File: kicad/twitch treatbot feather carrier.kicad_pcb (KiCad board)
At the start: 2 copper layers, 0 parts

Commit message: PCB floorplanning
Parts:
- added A1: Adafruit_Feather_HUZZAH_ESP8266, Module:Adafruit_Feather, F.Cu at (124.3, 100.4)
- added C1: 1000u/25V, Capacitor_THT:CP_Radial_D13.0mm_P5.00mm, F.Cu at (160.7, 133.2)
- added C2: 10u/25V, Capacitor_THT:CP_Radial_D8.0mm_P3.80mm, F.Cu at (198.0, 130.7)
- added C3: 10u, Capacitor_SMD:C_0805_2012Metric, F.Cu at (206.9, 131.9)
- added C4: 10u, Capacitor_SMD:C_0805_2012Metric, F.Cu at (197.2, 140.0)
- added C5: 1u, Capacitor_SMD:C_0805_2012Metric, F.Cu at (182.0, 158.8)
- added C6: 1000u/25V, Capacitor_THT:CP_Radial_D13.0mm_P5.00mm, F.Cu at (160.7, 147.8)
- added C7: 10u, Capacitor_SMD:C_0805_2012Metric, F.Cu at (197.2, 137.0)
- added C8: 10u, Capacitor_SMD:C_0805_2012Metric, F.Cu at (211.8, 127.4)
- added C9: 10u, Capacitor_SMD:C_0805_2012Metric, F.Cu at (197.2, 143.0)
- added D1: +12V, LED_SMD:LED_1206_3216Metric, F.Cu at (167.7, 156.7)
- added D2: +5V, LED_SMD:LED_1206_3216Metric, F.Cu at (182.6, 155.6)
- added D3: +3V3, LED_SMD:LED_1206_3216Metric, F.Cu at (167.7, 160.1)
- added J1: 128x64 OLED, Connector_PinSocket_2.54mm:PinSocket_1x04_P2.54mm_Vertical, F.Cu at (131.2, 149.9)
- added J2: Quiic MP3 Trigger [CHECK FOOTPRINT], Connector_PinSocket_2.54mm:PinSocket_1x04_P2.54mm_Vertical, F.Cu at (126.5, 149.4)
- added J3: M2, TerminalBlock:TerminalBlock_Altech_AK300-2_P5.00mm, F.Cu at (186.1, 132.9)
- added J4: M1, TerminalBlock:TerminalBlock_Altech_AK300-2_P5.00mm, F.Cu at (173.8, 146.9)
- added J5: NEO_PWR, TerminalBlock:TerminalBlock_Altech_AK300-2_P5.00mm, F.Cu at (186.1, 146.9)
- added J6: NEO_Signal, TerminalBlock:TerminalBlock_Altech_AK300-2_P5.00mm, F.Cu at (173.8, 132.9)
- added Q1: BSS138, Package_TO_SOT_SMD:SOT-23, F.Cu at (207.2, 128.2)
- added R1: 10k, Resistor_SMD:R_0805_2012Metric, F.Cu at (201.6, 142.8)
- added R2: 4k7, Resistor_SMD:R_0805_2012Metric, F.Cu at (211.8, 130.4)
- added R3: 1k, Resistor_SMD:R_0805_2012Metric, F.Cu at (186.4, 158.8)
- added R4: 10k, Resistor_SMD:R_0805_2012Metric, F.Cu at (187.6, 155.4)
- added R5: 1k, Resistor_SMD:R_0805_2012Metric, F.Cu at (216.3, 127.4)
- added R6: 1k, Resistor_SMD:R_0805_2012Metric, F.Cu at (206.9, 134.9)
- added R7: 10k, Resistor_SMD:R_0805_2012Metric, F.Cu at (201.6, 139.8)
- added RDNP1: 4k7, Resistor_SMD:R_0805_2012Metric, F.Cu at (197.2, 146.0)
- added SW1: ESP RESET, My Libraries:SW_Push_CK_PTS525_SM15, F.Cu at (175.1, 157.1)
- added SW2: Wiggle, My Libraries:SW_Push_CK_PTS525_SM15, F.Cu at (160.2, 158.2)
- added TP1: TestPoint_Harwin, My Libraries:Harwin-S1751-46-Test-Point, F.Cu at (201.6, 136.9)
- added U1: TMC2208_BREAKOUT, My Libraries:DIP-16_W12.7mm, F.Cu at (148.3, 95.3)

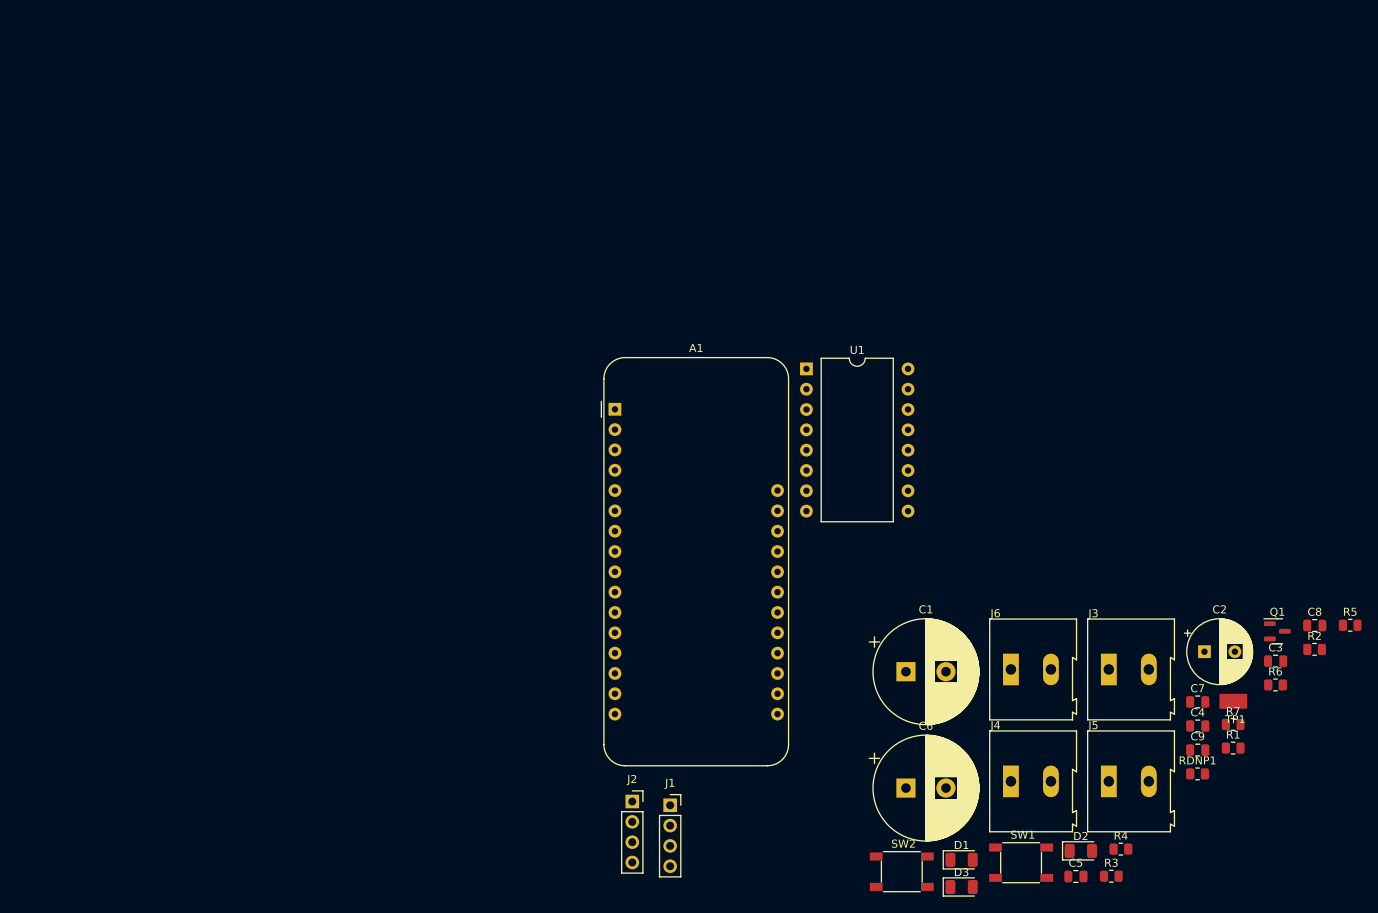
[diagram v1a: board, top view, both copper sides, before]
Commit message: first floorplan done
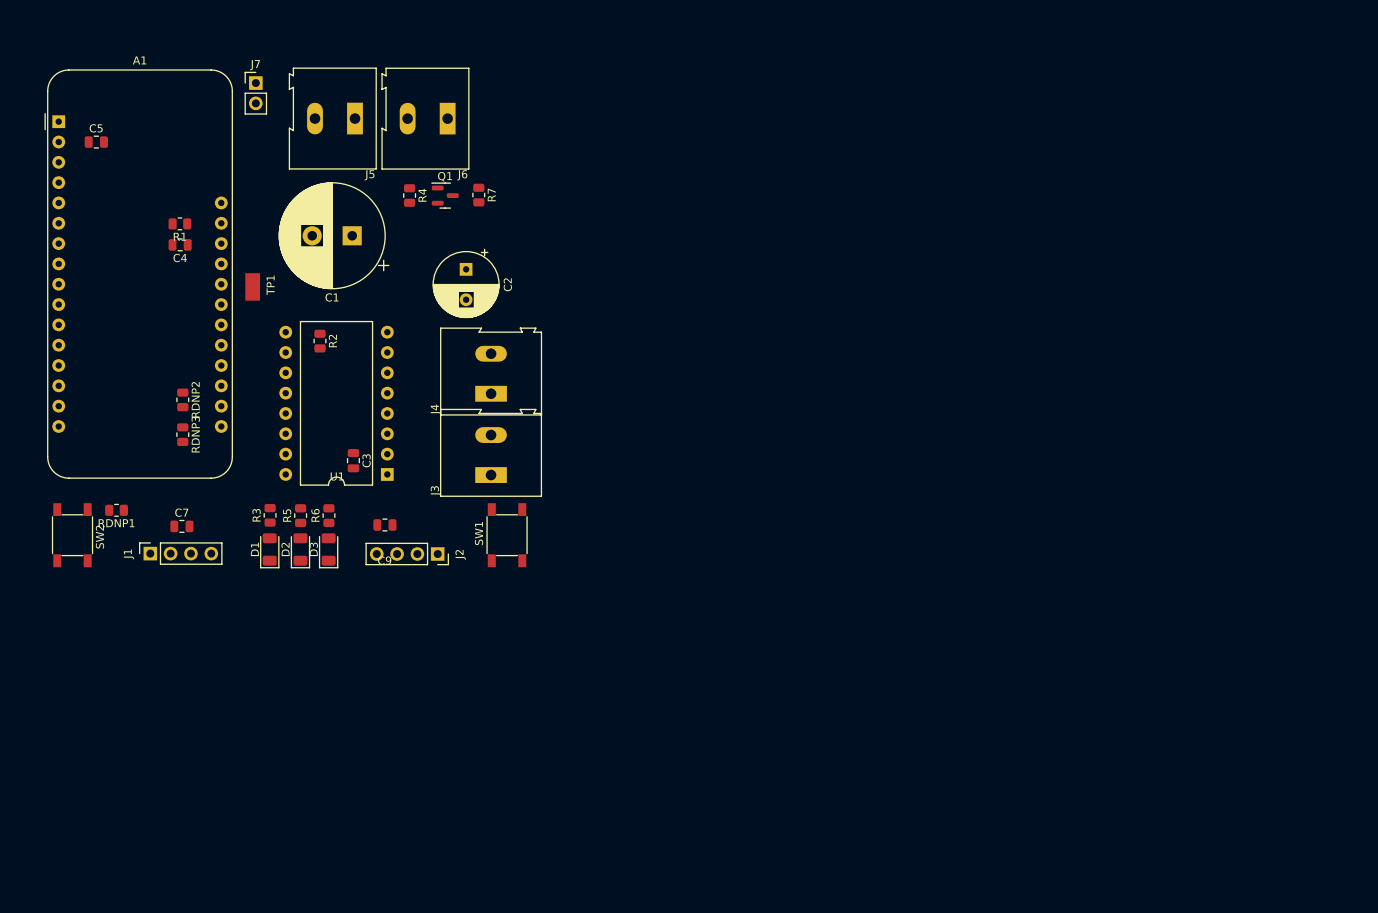
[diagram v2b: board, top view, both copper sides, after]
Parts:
- removed C6: 1000u/25V, Capacitor_THT:CP_Radial_D13.0mm_P5.00mm
- removed C8: 10u, Capacitor_SMD:C_0805_2012Metric
- added J7: +5V_IN, Connector_PinHeader_2.54mm:PinHeader_1x02_P2.54mm_Vertical, F.Cu at (79.5, 59.6)
- added RDNP2: 4k7, Resistor_SMD:R_0805_2012Metric, F.Cu at (70.3, 99.2)
- added RDNP3: 4k7, Resistor_SMD:R_0805_2012Metric, F.Cu at (70.3, 103.6)
- J5: value NEO_PWR -> +12V_IN
- moved C5 153.0 mm to (59.5, 67.0)
- moved R1 147.1 mm to (70.0, 77.2), turned to 180 degrees
- moved C4 140.7 mm to (70.0, 79.8), turned to 180 degrees
- moved RDNP1 139.1 mm to (62.0, 113.0), turned to 180 degrees
- moved TP1 133.1 mm to (79.1, 85.1), turned to 90 degrees
- moved R5 131.9 mm to (85.1, 113.7), turned to 90 degrees
- moved R2 130.2 mm to (87.5, 91.9), turned to -90 degrees
- moved C7 128.9 mm to (70.2, 115.0)
- moved J5 125.5 mm to (91.9, 64.1), turned to 180 degrees
- moved R4 120.8 mm to (98.7, 73.7), turned to -90 degrees
- moved R6 120.2 mm to (88.6, 113.7), turned to 90 degrees
- moved C3 118.0 mm to (91.7, 106.8), turned to -90 degrees
- moved Q1 117.4 mm to (103.1, 73.7)
- moved R7 115.2 mm to (107.3, 73.6), turned to -90 degrees
- moved R3 114.4 mm to (81.2, 113.7), turned to 90 degrees
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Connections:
- C9 pad 1: +5V -> +3V3
- J5 pad 1: +5V -> +12V

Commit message: 2nd floorplan
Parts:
- removed TP1: TestPoint_Harwin, My Libraries:Harwin-S1751-46-Test-Point
- moved A1 44.2 mm to (74.5, 104.0), turned to 180 degrees
- moved RDNP3 38.7 mm to (61.4, 65.9), turned to 180 degrees
- moved C5 33.7 mm to (70.1, 99.0), turned to 90 degrees
- moved RDNP2 30.5 mm to (61.4, 70.1), turned to 180 degrees
- moved R1 18.5 mm to (58.1, 91.4), turned to 0 degrees
- moved C4 14.9 mm to (58.1, 88.8), turned to 0 degrees
- moved C9 14.7 mm to (80.9, 114.9)
- moved J2 14.7 mm to (87.5, 118.6)
- moved D1 14.5 mm to (95.7, 118.4)
- moved D2 14.5 mm to (99.5, 118.4)
- moved D3 14.5 mm to (103.0, 118.4)
- moved R3 14.5 mm to (95.7, 114.2)
- moved R5 14.5 mm to (99.5, 114.2)
- moved R6 14.5 mm to (103.1, 114.2)
- moved J6 6.05 mm to (109.4, 65.0)
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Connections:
- A1 pad 11: /NEO_3v -> /STEP_DIR
- A1 pad 12: unconnected-(A1-Pad12) -> /STEP_STEP
- A1 pad 13: unconnected-(A1-Pad13) -> /STEP_EN
- A1 pad 15: unconnected-(A1-Pad15) -> /NEO_3v
- A1 pad 19: /STEP_EN -> unconnected-(A1-Pad19)
- A1 pad 20: /STEP_DIR -> unconnected-(A1-Pad20)
- A1 pad 22: /STEP_STEP -> unconnected-(A1-Pad22)
- A1 pad 23: /Wiggle -> unconnected-(A1-Pad23)
- A1 pad 24: Net-(A1-Pad24) -> unconnected-(A1-Pad24)
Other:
- board outline added: 66 x 66 mm

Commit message: Layout done, fully routed, most of silk done, debating if to convert to 2 layer board
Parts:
- added TP1: TestPoint_Harwin, My Libraries:Harwin-S1751-46-Test-Point, F.Cu at (108.9, 71.0)
- added TP2: TestPoint_Harwin, My Libraries:Harwin-S1751-46-Test-Point, F.Cu at (106.2, 71.0)
- added TP3: TestPoint_Harwin, My Libraries:Harwin-S1751-46-Test-Point, F.Cu at (81.9, 64.0)
- added TP4: TestPoint_Harwin, My Libraries:Harwin-S1751-46-Test-Point, F.Cu at (100.3, 110.2)
- moved D2 46.4 mm to (54.0, 109.8), turned to -90 degrees
- moved R5 46.3 mm to (54.0, 105.6)
- moved D3 42.6 mm to (61.3, 109.8), turned to -90 degrees
- moved R6 42.6 mm to (61.3, 105.6)
- moved D1 38.9 mm to (57.7, 109.9), turned to -90 degrees
- moved R3 38.9 mm to (57.8, 105.7)
- moved C7 14.0 mm to (81.9, 107.4), turned to 180 degrees
- moved SW2 13.5 mm to (68.3, 109.5), turned to 0 degrees
- moved J1 12.4 mm to (75.7, 110.3)
- moved J2 11.5 mm to (95.6, 110.4)
- moved J4 11.5 mm to (104.5, 87.0), turned to -90 degrees
- moved J3 11.5 mm to (104.5, 97.2), turned to -90 degrees
- moved RDNP1 10.8 mm to (68.3, 104.2)
- moved C9 10.5 mm to (88.3, 107.4)
- moved J5 9.13 mm to (88.0, 62.2), turned to 0 degrees
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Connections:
- net Net-(A1-Pad1) renamed /~{RESET}
- A1 pad 22: unconnected-(A1-Pad22) -> /Wiggle
- J1 pad 4: /5V -> +5V
- J2 pad 3: /3v3 -> +3V3
- J3 pad 1: /M2B -> /M2A
- J3 pad 2: /M2A -> /M2B
- J4 pad 1: /M1A -> /M1B
- J4 pad 2: /M1B -> /M1A
- J5 pad 1: +12V -> GND
- J5 pad 2: GND -> +12V
- J6 pad 1: /NEO_5v -> GND
- J6 pad 2: GND -> /NEO_5v
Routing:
- net /SCL: track 0.00 -> 92.7 mm
- net /SDA: track 0.00 -> 90.3 mm
- net +3V3: track 0.00 -> 82.4 mm, vias 0 -> 7
- net +12V: track 0.00 -> 59.9 mm, vias 0 -> 1
- net /NEO_3v: track 0.00 -> 58.0 mm
- net /Wiggle: track 0.00 -> 55.4 mm
- net +5V: track 0.00 -> 46.3 mm, vias 0 -> 4
- net /~{RESET}: track 0.00 -> 44.9 mm
- net /STEP_STEP: track 0.00 -> 39.3 mm
- net /STEP_DIR: track 0.00 -> 38.7 mm
- net /STEP_EN: track 0.00 -> 30.5 mm
- net /NEO_5v: track 0.00 -> 17.4 mm
- net GND: track 0.00 -> 3.36 mm, vias 0 -> 18
- net Net-(D2-Pad1): track 0.00 -> 1.94 mm
- net Net-(D3-Pad1): track 0.00 -> 1.90 mm
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- added copper zone on B.Cu, net +12V
- added copper zone on B.Cu, net +3V3
- added copper zone on F.Cu, net +3V3
- added copper zone on B.Cu, net +5V
- added copper zone on F.Cu, net +5V
- added copper zone on In2.Cu, net +5V
- added copper zone on F.Cu, net /M1A
- added copper zone on F.Cu, net /M1B
- added copper zone on F.Cu, net /M2A
- added copper zone on F.Cu, net /M2B
- added copper zone on B.Cu, net GND
- added copper zone on F.Cu, net GND
- added copper zone on In1.Cu, net GND
- added copper zone on In2.Cu, net GND
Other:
- board size 66 x 66 mm -> 59.8 x 58.1 mm
- copper layers 2 -> 4
- board text added: "+12V"
- board text added: "+5V"
- board text added: "12V"
- board text added: "12v"
- board text added: "3v"
- board text added: "5V"
- board text added: "BRN"
- board text added: "ESP RESET"
- board text added: "GRN"
- board text added: "NEO"
- board text added: "Neo Data"
- board text added: "OLED"
- board text added: "Qwicc MP3"
- board text added: "RED"
- board text added: "SCL"
- board text added: "SDA"
- board text added: "S_DIR"
- board text added: "S_EN"
- board text added: "S_STP"
- board text added: "Wiggle"
- board text added: "YLW"
- board text added: "~{RES}"

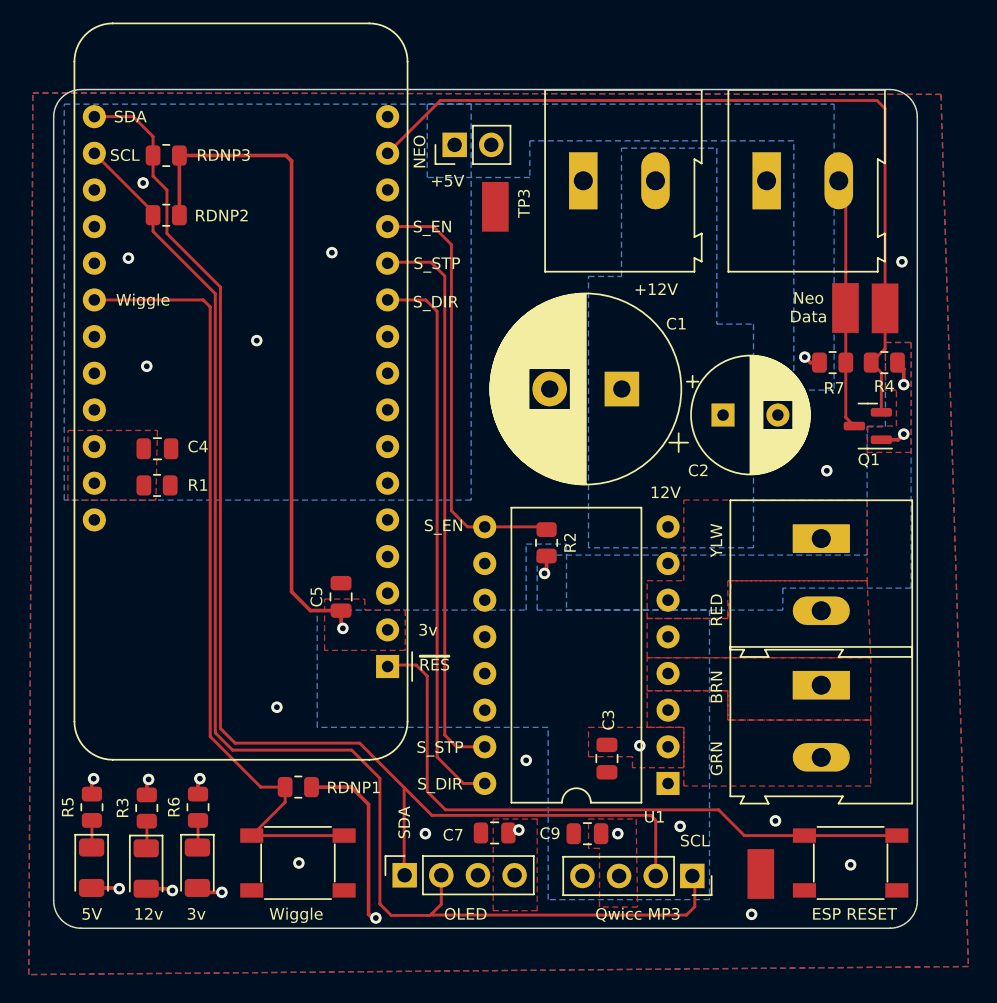
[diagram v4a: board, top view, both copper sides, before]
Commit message: forgot mounting holes!
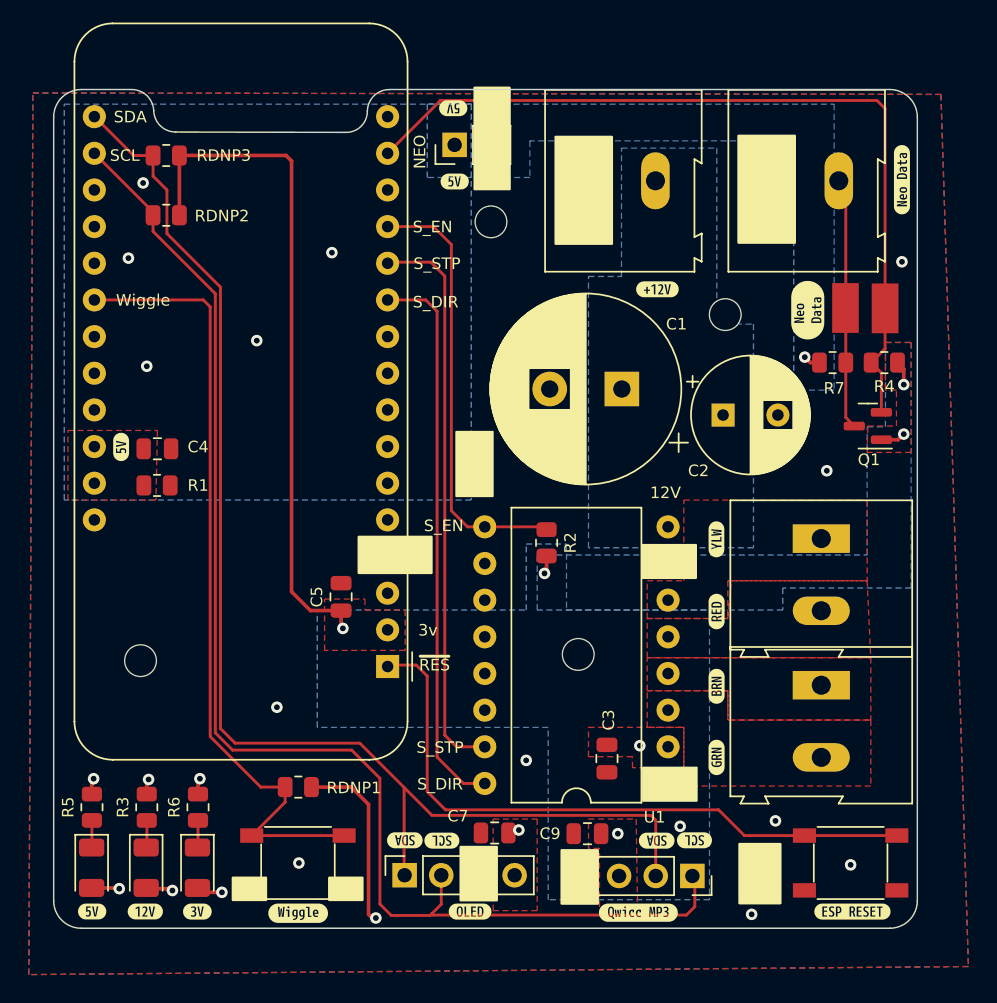
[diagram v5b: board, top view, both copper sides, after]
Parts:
- added H1: MountingHole, MountingHole:MountingHole_2.2mm_M2, F.Cu at (97.9, 71.5)
- added H2: MountingHole, MountingHole:MountingHole_2.2mm_M2, F.Cu at (87.7, 95.0)
- added H3: MountingHole, MountingHole:MountingHole_2.2mm_M2, F.Cu at (81.6, 65.0)
- added H4: MountingHole, MountingHole:MountingHole_2.2mm_M2, F.Cu at (57.4, 95.5)
- added kibuzzard-622632CA: G***, kibuzzard-622632CA, F.Cu at (61.3, 112.8)
- added kibuzzard-622632E6: G***, kibuzzard-622632E6, F.Cu at (57.7, 112.8)
- added kibuzzard-622632F0: G***, kibuzzard-622632F0, F.Cu at (54.0, 112.8)
- added kibuzzard-622632F0: G***, kibuzzard-622632F0, F.Cu at (56.0, 80.6)
- added kibuzzard-622632F0: G***, kibuzzard-622632F0, B.Cu at (56.0, 80.6)
- added kibuzzard-622632F9: G***, kibuzzard-622632F9, F.Cu at (68.3, 113.0)
- added kibuzzard-6226330D: G***, kibuzzard-6226330D, F.Cu at (80.2, 112.8)
- added kibuzzard-6226330D: G***, kibuzzard-6226330D, B.Cu at (80.2, 112.8)
- added kibuzzard-6226331D: G***, kibuzzard-6226331D, F.Cu at (91.8, 112.9)
- added kibuzzard-6226331D: G***, kibuzzard-6226331D, B.Cu at (91.8, 112.9)
- added kibuzzard-62263363: G***, kibuzzard-62263363, F.Cu at (106.7, 112.8)
- added kibuzzard-62263378: G***, kibuzzard-62263378, F.Cu at (95.7, 107.9)
- added kibuzzard-62263378: G***, kibuzzard-62263378, F.Cu at (78.2, 107.9)
- added kibuzzard-62263378: G***, kibuzzard-62263378, B.Cu at (78.2, 107.9)
- added kibuzzard-62263378: G***, kibuzzard-62263378, B.Cu at (95.7, 107.9)
- added kibuzzard-62263388: G***, kibuzzard-62263388, F.Cu at (75.7, 107.9)
- added kibuzzard-62263388: G***, kibuzzard-62263388, F.Cu at (93.1, 107.9)
- added kibuzzard-62263388: G***, kibuzzard-62263388, B.Cu at (75.7, 107.9)
- added kibuzzard-62263388: G***, kibuzzard-62263388, B.Cu at (93.1, 107.9)
- added kibuzzard-622633E5: G***, kibuzzard-622633E5, F.Cu at (97.3, 102.2)
- added kibuzzard-622633E5: G***, kibuzzard-622633E5, B.Cu at (97.3, 102.2)
- added kibuzzard-622633FA: G***, kibuzzard-622633FA, F.Cu at (97.3, 92.0)
- added kibuzzard-622633FA: G***, kibuzzard-622633FA, B.Cu at (97.3, 92.0)
- added kibuzzard-62263418: G***, kibuzzard-62263418, F.Cu at (97.3, 97.2)
- added kibuzzard-62263418: G***, kibuzzard-62263418, B.Cu at (97.3, 97.2)
- added kibuzzard-62263431: G***, kibuzzard-62263431, F.Cu at (97.3, 87.0)
- added kibuzzard-62263431: G***, kibuzzard-62263431, B.Cu at (97.3, 87.0)
- added kibuzzard-62263473: G***, kibuzzard-62263473, F.Cu at (103.6, 71.2)
- added kibuzzard-62263481: G***, kibuzzard-62263481, F.Cu at (110.1, 62.1)
- added kibuzzard-62263481: G***, kibuzzard-62263481, B.Cu at (105.8, 58.8)
- added kibuzzard-62263491: G***, kibuzzard-62263491, F.Cu at (93.2, 69.7)
- added kibuzzard-62263491: G***, kibuzzard-62263491, B.Cu at (93.1, 58.9)
- added kibuzzard-622634A8: G***, kibuzzard-622634A8, F.Cu at (79.0, 57.2)
- added kibuzzard-622634A8: G***, kibuzzard-622634A8, F.Cu at (79.1, 62.3)
- added kibuzzard-622634A8: G***, kibuzzard-622634A8, B.Cu at (79.0, 57.2)
- added kibuzzard-622634A8: G***, kibuzzard-622634A8, B.Cu at (79.1, 62.3)
- moved TP3 17.8 mm to (80.5, 81.7)
- moved D1 0.05 mm to (57.7, 109.8)
- moved R3 0.05 mm to (57.8, 105.6)
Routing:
- net /SDA: track 90.3 -> 89.6 mm
- net GND: vias 18 -> 17
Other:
- outline, holes or cut-outs redrawn
- board text removed: "+12V"
- board text removed: "+5V"
- board text removed: "12v"
- board text removed: "5V"
- board text removed: "BRN"
- board text removed: "ESP RESET"
- board text removed: "GRN"
- board text removed: "Neo Data"
- board text removed: "OLED"
- board text removed: "Qwicc MP3"
- board text removed: "RED"
- board text removed: "YLW"
